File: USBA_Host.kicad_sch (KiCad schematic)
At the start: 90 parts, among them J4 UAA112C-84168-4H, J5 UAA112C-84168-4H, U1 SY6280AAAC, U11 RTS5411S-GR, U3 SY6280AAAC, U4 SY6280AAAC, U40 ICMEF112P900MFR, U42 ICMEF112P900MFR, U44 ICMEF112P900MFR, U45 ICMEF112P900MFR, U48 TPD4E05U06DQAR, U49 TPD4E05U06DQAR, U50 TPD4E05U06DQAR, U51 TPD4E05U06DQAR, U9 SY6280AAAC, Y8 K3A120002010

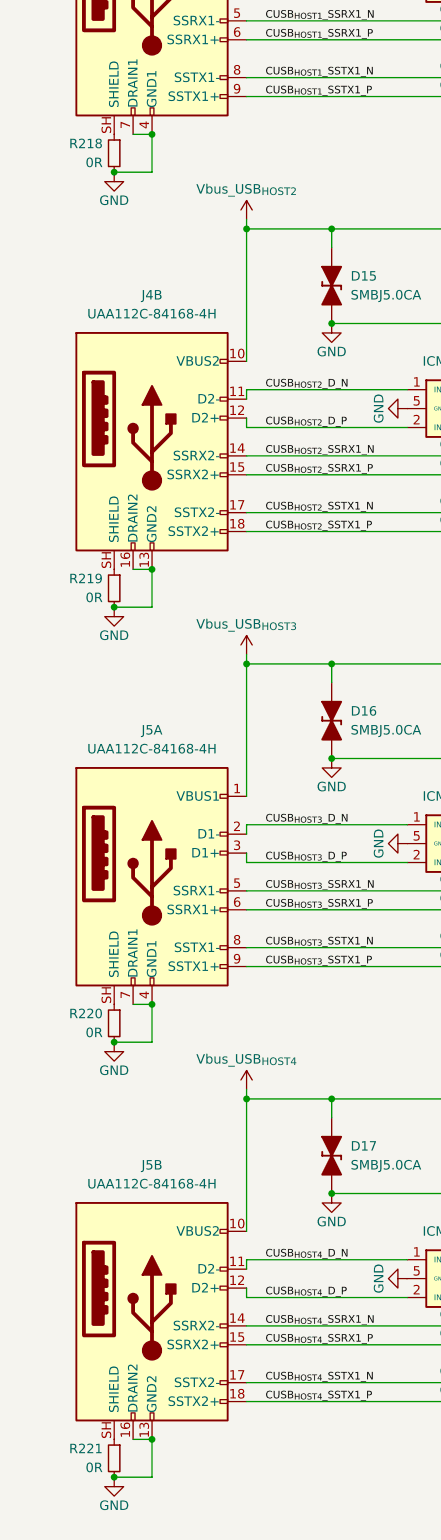
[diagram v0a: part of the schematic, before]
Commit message: Replace v2 with updated RK3576_SBCv2 (Copy) Oct 2
- Update 18 sheets to Oct 2 15:37 local versions
- Keep cleaned layout: exclude .history/, Resources/, *.bak, *.lck,
  project.kicad_dru, .hs_rules.json, lowercase dup placeholders
  (fixtures/power), empty orphans (digital, mechanical, output,
  USBC_MCU, eMMC_UFS)
- Preserve LICENSE, README.md, .gitignore
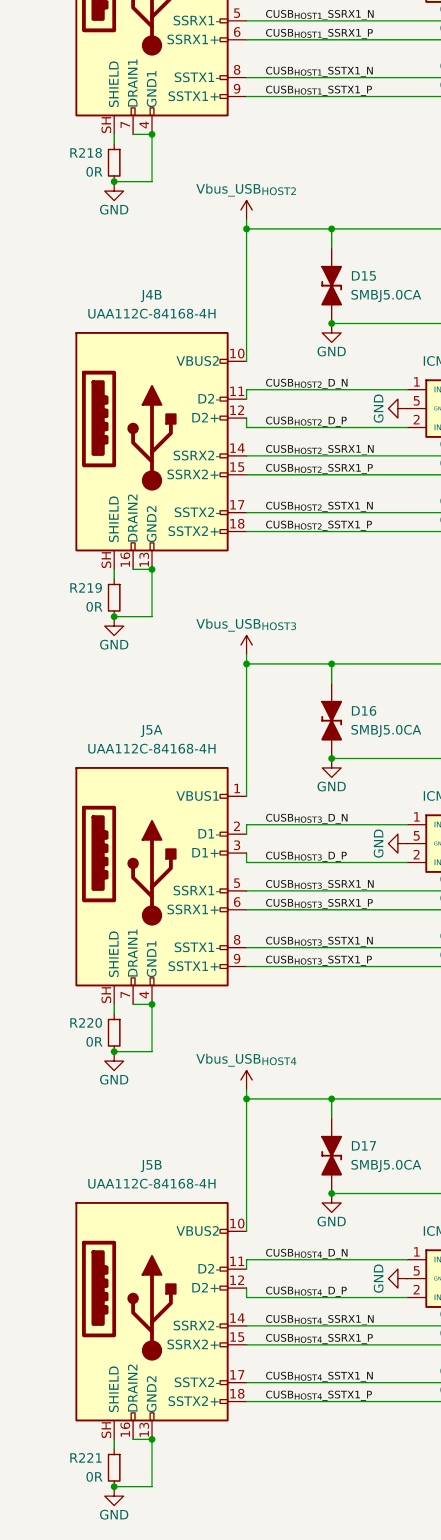
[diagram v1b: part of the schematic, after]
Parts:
- C226, C227: footprint Capacitor_SMD:C_0402_1005Metric_Pad0.74x0.62mm_HandSolder -> Capacitor_SMD:C_0402_1005Metric
- C402, C403, C404, C405, C406, C407, C408, C409: Mouser Part 187-CL03A104KO3NNNC -> 187-CL03A104KO3NNND
- R226, R237, R238, R242, R245, R248: LCSC Part C60491 -> C60490; Mouser Part 603-RC0402FR-07100KL -> 603-RC0402FR-0710KL
- U1, U3, U4, U9: LCSC Part (none) -> C207620
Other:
- moved on the sheet: R218, R219, R220, R221

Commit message: Relink hierarchical root: 18 sheets into RK3576 SBCv2 top level
Root was empty (no sheet boxes); all subsheets orphaned.
Rebuilt A1 top level linking RK3576, LPDDR5, Power, Ethernet,
HDMI, MIPI, PCIe, USB-A/C, Wireless, RTC, uSD, GPIO, OLED,
RP2350A, Connectors, Fixtures, DC_Power. block_diagrame kept
docs-only (unlinked, avoids double-instantiation). Lowercase
stub duplicates excluded. ERC: 1388 -> 770 violations.
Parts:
- removed J4, J5: UAA112C-84168-4H, Connector_USB:USB3_A_Molex_48406-0001_Horizontal_Stacked, symbol Connector:USB3_A_Stacked
- added J6, J7: UAA112C-84168-4H, #kicad Library:USB3_A_Molex_48406-0001_Horizontal_Stacked, symbol Connector:USB3_A_Stacked
- renumbered C190 to C149, C205 to C150, C215 to C151, C225 to C152, C195 to C153, C196 to C154, C197 to C155, C201 to C156, C219 to C157, C220 to C158, C221 to C159, C223 to C160, C402 to C161, C403 to C162, C404 to C163, C405 to C164, C406 to C165, C407 to C166, C408 to C167, C409 to C168, C189 to C169, C214 to C170, C224 to C171, C229 to C172, C198 to C173, C199 to C174, C222 to C175, C191 to C176, C206 to C177, C192 to C178, C202 to C179, C216 to C180, C226 to C181, C207 to C182, C193 to C183, C203 to C184, C217 to C185, C208 to C186, C194 to C187, C204 to C188, C218 to C189, C227 to C190, C209 to C191, C210 to C192, C228 to C193, C212 to C194, C213 to C195, C399 to C196, D16 to D10, D17 to D11, D10 to D8, D15 to D9, R218 to R56, R219 to R57, R220 to R58, R221 to R59, R222 to R60, R241 to R61, R244 to R62, R247 to R63, R226 to R64, R242 to R65, R245 to R66, R248 to R67, R230 to R68, R243 to R69, R246 to R70, R249 to R71, R234 to R72, R235 to R73, R86 to R74, R88 to R75, R238 to R76, R237 to R77, U40 to U11, U42 to U12, U44 to U13, U45 to U14, U1 to U15, U3 to U16, U4 to U17, U9 to U18, U48 to U19, U49 to U20, U50 to U21, U11 to U22, U51 to U23, Y8 to Y4
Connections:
- net CUSB_{HOST1}_D_N: now also J6.2 (D1-)
- net CUSB_{HOST1}_D_P: now also J6.3 (D1+)
- net CUSB_{HOST1}_SSRX1_N: now also J6.5 (SSRX1-)
- net CUSB_{HOST1}_SSRX1_P: now also J6.6 (SSRX1+)
- net CUSB_{HOST1}_SSTX1_N: now also J6.8 (SSTX1-)
- net CUSB_{HOST1}_SSTX1_P: now also J6.9 (SSTX1+)
- net CUSB_{HOST2}_D_N: now also J6.11 (D2-)
- net CUSB_{HOST2}_D_P: now also J6.12 (D2+)
- net CUSB_{HOST2}_SSRX1_N: now also J6.14 (SSRX2-)
- net CUSB_{HOST2}_SSRX1_P: now also J6.15 (SSRX2+)
- net CUSB_{HOST2}_SSTX1_N: now also J6.17 (SSTX2-)
- net CUSB_{HOST2}_SSTX1_P: now also J6.18 (SSTX2+)
- net CUSB_{HOST3}_D_N: now also J7.2 (D1-)
- net CUSB_{HOST3}_D_P: now also J7.3 (D1+)
- net CUSB_{HOST3}_SSRX1_N: now also J7.5 (SSRX1-)
- net CUSB_{HOST3}_SSRX1_P: now also J7.6 (SSRX1+)
- net CUSB_{HOST3}_SSTX1_N: now also J7.8 (SSTX1-)
- net CUSB_{HOST3}_SSTX1_P: now also J7.9 (SSTX1+)
- net CUSB_{HOST4}_D_N: now also J7.11 (D2-)
- net CUSB_{HOST4}_D_P: now also J7.12 (D2+)
- net CUSB_{HOST4}_SSRX1_N: now also J7.14 (SSRX2-)
- net CUSB_{HOST4}_SSRX1_P: now also J7.15 (SSRX2+)
- net CUSB_{HOST4}_SSTX1_N: now also J7.17 (SSTX2-)
- net CUSB_{HOST4}_SSTX1_P: now also J7.18 (SSTX2+)
- net GND: now also J6.13 (GND2), J6.16 (DRAIN2), J6.4 (GND1), J6.7 (DRAIN1), J7.13 (GND2), J7.16 (DRAIN2), J7.4 (GND1), J7.7 (DRAIN1)
- net Vbus_USB_{HOST1}: now also J6.1 (VBUS1)
- net Vbus_USB_{HOST2}: now also J6.10 (VBUS2)
- net Vbus_USB_{HOST3}: now also J7.1 (VBUS1)
- net Vbus_USB_{HOST4}: now also J7.10 (VBUS2)
- net at R57.1: now also J6.SH (SHIELD)
- net at R58.1: now also J7.SH (SHIELD)
- net at R59.1: now also J7.SH (SHIELD)
- net at R56.1: now also J6.SH (SHIELD)

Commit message: block diagrame with Hierarchical labels and NVMe SSD footprint
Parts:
- renumbered C181 to C180, C182 to C181, C183 to C182, C184 to C183, C186 to C184, C187 to C185, C188 to C186, C180 to C187, C190 to C188, C191 to C189, C185 to C190, C192 to C191, C189 to C192, D8 to D24, D9 to D25, D10 to D26, D11 to D27
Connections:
- net CUSB_{HOST1}_SSRX1_N: now also U19.10 (NC)
- net CUSB_{HOST1}_SSRX1_P: now also U19.9 (NC)
- net CUSB_{HOST1}_SSTX1_N: now also U19.7 (NC)
- net CUSB_{HOST1}_SSTX1_P: now also U19.6 (NC)
- net CUSB_{HOST2}_SSRX1_N: now also U23.10 (NC)
- net CUSB_{HOST2}_SSRX1_P: now also U23.9 (NC)
- net CUSB_{HOST2}_SSTX1_N: now also U23.7 (NC)
- net CUSB_{HOST2}_SSTX1_P: now also U23.6 (NC)
- net CUSB_{HOST3}_SSRX1_N: now also U20.10 (NC)
- net CUSB_{HOST3}_SSRX1_P: now also U20.9 (NC)
- net CUSB_{HOST3}_SSTX1_N: now also U20.7 (NC)
- net CUSB_{HOST3}_SSTX1_P: now also U20.6 (NC)
- net CUSB_{HOST4}_SSRX1_N: now also U21.10 (NC)
- net CUSB_{HOST4}_SSRX1_P: now also U21.9 (NC)
- net CUSB_{HOST4}_SSTX1_N: now also U21.7 (NC)
- net CUSB_{HOST4}_SSTX1_P: now also U21.6 (NC)
- net USB_{HUB}_D_N renamed USB_{HUB}.D_N
- net USB_{HUB}_D_P renamed USB_{HUB}.D_P
- net USB_{HUB}_SSRX1_N renamed USB_{HUB}.SSRX1_N
- net USB_{HUB}_SSRX1_P renamed USB_{HUB}.SSRX1_P
- net USB_{HUB}_SSTX1_N renamed USB_{HUB}.SSTX1_N
- net USB_{HUB}_SSTX1_P renamed USB_{HUB}.SSTX1_P
- no-connect marks 35 -> 19
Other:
- moved on the sheet: C175, C187, C190, C192, R74, R75, R76, R77
